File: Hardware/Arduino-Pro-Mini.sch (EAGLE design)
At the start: 26 parts, among them Q1 8/16/20MHz, U1 ATMEGA328, U2 MIC5205

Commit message: Fixed schematic issues
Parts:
- Q1: value 8/16/20MHz -> 8/16MHz
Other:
- note added: "Original Arduino Mini Design by Team Arduino Arduino Pro Mini Design by SparkFun Electronics Revised by: Marshall Taylor"
- note removed: "Original Arduino Mini Design by Team Arduino Arduino Pro Mini Design by Spark Fun Electronics Revised by: Marshall Taylor"
- moved on the sheet: R1, R3
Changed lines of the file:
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@@
 </part>
 <part name="JP3" library="SparkFun" deviceset="M02" device="PTH"/>
-<part name="Q1" library="SparkFun" deviceset="RESONATOR" device="1:1" value="8/16/20MHz">
+<part name="Q1" library="SparkFun" deviceset="RESONATOR" device="1:1" value="8/16MHz">
 <attribute name="PROD_ID" value="XTAL-08900"/>
 </part>
@@
 </polygon>
 <text x="167.64" y="13.462" size="1.524" layer="94" font="vector" align="top-left">Original Arduino Mini Design by Team Arduino
-Arduino Pro Mini Design by Spark Fun Electronics
+Arduino Pro Mini Design by SparkFun Electronics
 Revised by: Marshall Taylor</text>
 </plain>
@@
 </instance>
 <instance part="JP6" gate="G$1" x="101.6" y="25.4" smashed="yes" rot="R180">
-<attribute name="VALUE" x="101.6" y="45.72" size="1.778" layer="96" font="vector" rot="R180"/>
 <attribute name="NAME" x="101.6" y="9.398" size="1.778" layer="95" font="vector" rot="R180"/>
 </instance>
 <instance part="JP7" gate="G$1" x="43.18" y="27.94" smashed="yes">
-<attribute name="VALUE" x="43.18" y="7.62" size="1.778" layer="96" font="vector"/>
 <attribute name="NAME" x="43.18" y="43.942" size="1.778" layer="95" font="vector"/>
 </instance>
@@
 </instance>
 <instance part="JP1" gate="G$1" x="17.78" y="25.4" smashed="yes">
-<attribute name="VALUE" x="12.7" y="15.24" size="1.778" layer="96" font="vector"/>
+<attribute name="VALUE" x="7.62" y="15.24" size="1.778" layer="96" font="vector"/>
 <attribute name="NAME" x="12.7" y="36.322" size="1.778" layer="95" font="vector"/>
 </instance>
@@
 <attribute name="PROD_ID" x="114.3" y="149.86" size="1.27" layer="96" font="vector" rot="R270" display="off"/>
 </instance>
-<instance part="R1" gate="G$1" x="210.82" y="147.32" smashed="yes" rot="R90">
-<attribute name="NAME" x="209.3214" y="143.51" size="1.778" layer="95" font="vector" rot="R90"/>
-<attribute name="VALUE" x="214.122" y="143.51" size="1.778" layer="96" rot="R90"/>
-</instance>
-<instance part="R3" gate="G$1" x="215.9" y="144.78" smashed="yes" rot="R90">
-<attribute name="NAME" x="214.4014" y="140.97" size="1.778" layer="95" font="vector" rot="R90"/>
-<attribute name="VALUE" x="219.202" y="140.97" size="1.778" layer="96" rot="R90"/>
+<instance part="R1" gate="G$1" x="210.82" y="149.86" smashed="yes" rot="R90">
+<attribute name="NAME" x="209.3214" y="146.05" size="1.778" layer="95" font="vector" rot="R90"/>
+<attribute name="VALUE" x="214.122" y="146.05" size="1.778" layer="96" rot="R90"/>
+</instance>
+<instance part="R3" gate="G$1" x="215.9" y="149.86" smashed="yes" rot="R90">
+<attribute name="NAME" x="214.4014" y="146.05" size="1.778" layer="95" font="vector" rot="R90"/>
+<attribute name="VALUE" x="219.202" y="146.05" size="1.778" layer="96" rot="R90"/>
 </instance>
 <instance part="P+2" gate="G$1" x="210.82" y="157.48" smashed="yes">
@@
 <instance part="Q1" gate="G$1" x="147.32" y="121.92" smashed="yes" rot="R270">
 <attribute name="NAME" x="143.764" y="125.73" size="1.778" layer="95" font="vector"/>
-<attribute name="VALUE" x="137.922" y="116.332" size="1.778" layer="96" font="vector"/>
+<attribute name="VALUE" x="140.462" y="116.332" size="1.778" layer="96" font="vector"/>
 <attribute name="PROD_ID" x="147.32" y="121.92" size="1.27" layer="96" font="vector" rot="R270" display="off"/>
 </instance>
@@
 </segment>
 <segment>
-<wire x1="210.82" y1="152.4" x2="210.82" y2="157.48" width="0.1524" layer="91"/>
+<wire x1="210.82" y1="154.94" x2="210.82" y2="157.48" width="0.1524" layer="91"/>
 <pinref part="P+2" gate="G$1" pin="3.3V"/>
 <pinref part="R1" gate="G$1" pin="2"/>
 </segment>
 <segment>
-<wire x1="215.9" y1="149.86" x2="215.9" y2="157.48" width="0.1524" layer="91"/>
+<wire x1="215.9" y1="154.94" x2="215.9" y2="157.48" width="0.1524" layer="91"/>
 <pinref part="P+3" gate="G$1" pin="3.3V"/>
 <pinref part="R3" gate="G$1" pin="2"/>
@@
 <segment>
 <wire x1="198.12" y1="137.16" x2="215.9" y2="137.16" width="0.1524" layer="91"/>
-<wire x1="215.9" y1="137.16" x2="215.9" y2="139.7" width="0.1524" layer="91"/>
+<wire x1="215.9" y1="137.16" x2="215.9" y2="144.78" width="0.1524" layer="91"/>
 <pinref part="U1" gate="G$1" pin="PC5(ADC5/SCL)"/>
 <pinref part="R3" gate="G$1" pin="1"/>
+<wire x1="215.9" y1="137.16" x2="220.98" y2="137.16" width="0.1524" layer="91"/>
+<label x="220.98" y="137.16" size="1.27" layer="95" xref="yes"/>
+<junction x="215.9" y="137.16"/>
 </segment>
 </net>
@@
 <segment>
 <wire x1="198.12" y1="139.7" x2="210.82" y2="139.7" width="0.1524" layer="91"/>
-<wire x1="210.82" y1="139.7" x2="210.82" y2="142.24" width="0.1524" layer="91"/>
+<wire x1="210.82" y1="139.7" x2="210.82" y2="144.78" width="0.1524" layer="91"/>
 <pinref part="U1" gate="G$1" pin="PC4(ADC4/SDA)"/>
 <pinref part="R1" gate="G$1" pin="1"/>
+<wire x1="210.82" y1="139.7" x2="220.98" y2="139.7" width="0.1524" layer="91"/>
+<label x="220.98" y="139.7" size="1.27" layer="95" xref="yes"/>
+<junction x="210.82" y="139.7"/>
 </segment>
 </net>

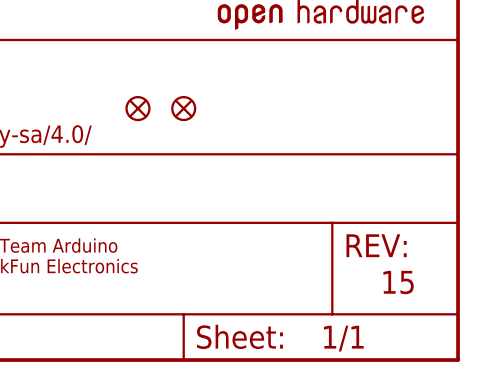
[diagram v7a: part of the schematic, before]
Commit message: Re-imported silk graphics, moved a couple ground vias, incremented version number to 1.6
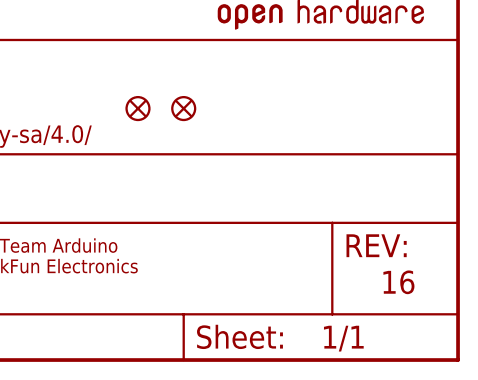
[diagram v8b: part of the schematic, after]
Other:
- note added: "16"
- note removed: "15"
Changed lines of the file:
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@@
 <text x="217.678" y="149.86" size="1.778" layer="97" font="vector">Optional
 I2C Pull-ups</text>
-<text x="240.284" y="7.366" size="2.54" layer="94" font="vector">15</text>
+<text x="240.284" y="7.366" size="2.54" layer="94" font="vector">16</text>
 <text x="7.62" y="119.38" size="1.778" layer="97" font="vector" align="top-left">Power isolation jumper SJ1:
  Open to source mini from
